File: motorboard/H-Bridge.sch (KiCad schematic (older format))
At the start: 5 parts

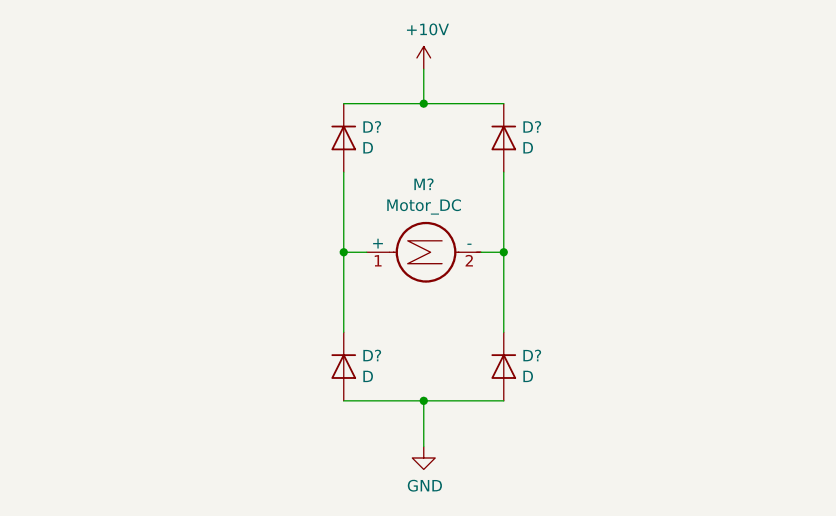
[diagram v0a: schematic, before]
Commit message: basic h bridge complete
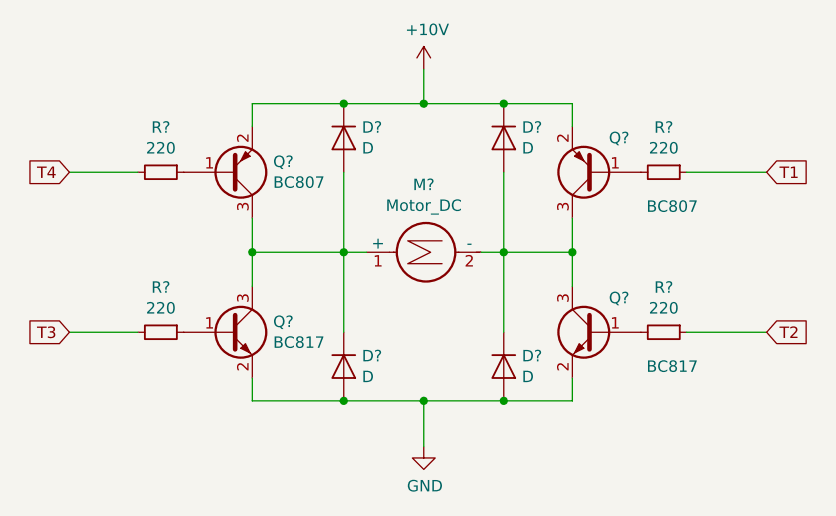
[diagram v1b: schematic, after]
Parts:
- added Q? (x2): BC807, Package_TO_SOT_SMD:SOT-23, symbol Transistor_BJT:BC807
- added Q? (x2): BC817, Package_TO_SOT_SMD:SOT-23, symbol Transistor_BJT:BC817
- added R? (x4): 220, symbol Device:R_Small
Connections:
- net +10V: now also Q?.2 (E), Q?.2 (E)
- net GND: now also Q?.2 (E), Q?.2 (E)
- net at D?.1 (K), D?.2 (A), M?.1 (+): now also Q?.3 (C), Q?.3 (C)
- net at D?.1 (K), D?.2 (A), M?.2 (-): now also Q?.3 (C), Q?.3 (C)
- new net: Q?.1 (B), R?.1 (x2)
- new net: Q?.1 (B), R?.2 (x2)
- new net T1: R?.1
- new net T2: R?.1
- new net T3: R?.2
- new net T4: R?.2
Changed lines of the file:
@@
 U 1 1 5E41C8CC
 P 3800 3350
+AR Path="/5E41C8CC" Ref="M?"  Part="1"
+AR Path="/5E41532A/5E41C8CC" Ref="M?"  Part="1"
 F 0 "M?" V 4095 3300 50  0000 C CNN
 F 1 "Motor_DC" V 4004 3300 50  0000 C CNN
@@
 U 1 1 5E41C8D2
 P 3500 2850
+AR Path="/5E41C8D2" Ref="D?"  Part="1"
+AR Path="/5E41532A/5E41C8D2" Ref="D?"  Part="1"
 F 0 "D?" V 3454 2929 50  0000 L CNN
 F 1 "D" V 3545 2929 50  0000 L CNN
@@
 U 1 1 5E41C8D8
 P 4200 2850
+AR Path="/5E41C8D8" Ref="D?"  Part="1"
+AR Path="/5E41532A/5E41C8D8" Ref="D?"  Part="1"
 F 0 "D?" V 4154 2929 50  0000 L CNN
 F 1 "D" V 4245 2929 50  0000 L CNN
@@
 U 1 1 5E41C8DE
 P 3500 3850
+AR Path="/5E41C8DE" Ref="D?"  Part="1"
+AR Path="/5E41532A/5E41C8DE" Ref="D?"  Part="1"
 F 0 "D?" V 3454 3929 50  0000 L CNN
 F 1 "D" V 3545 3929 50  0000 L CNN
@@
 U 1 1 5E41C8E4
 P 4200 3850
+AR Path="/5E41C8E4" Ref="D?"  Part="1"
+AR Path="/5E41532A/5E41C8E4" Ref="D?"  Part="1"
 F 0 "D?" V 4154 3929 50  0000 L CNN
 F 1 "D" V 4245 3929 50  0000 L CNN
@@
 U 1 1 5E41C8EA
 P 3850 4200
+AR Path="/5E41C8EA" Ref="#PWR?"  Part="1"
+AR Path="/5E41532A/5E41C8EA" Ref="#PWR?"  Part="1"
 F 0 "#PWR?" H 3850 3950 50  0001 C CNN
 F 1 "GND" H 3855 4027 50  0000 C CNN
@@
 AR Path="/5DAD2180/5E41C8F0" Ref="#PWR?"  Part="1"
 AR Path="/5E41C8F0" Ref="#PWR?"  Part="1"
+AR Path="/5E41532A/5E41C8F0" Ref="#PWR?"  Part="1"
 F 0 "#PWR?" H 3850 2400 50  0001 C CNN
 F 1 "+10V" H 3865 2723 50  0000 C CNN
@@
 Wire Wire Line
 	3850 4000 4200 4000
+$Comp
+L Transistor_BJT:BC807 Q?
+U 1 1 5E420AAC
+P 3000 3000
+F 0 "Q?" H 3191 2954 50  0000 L CNN
+F 1 "BC807" H 3191 3045 50  0000 L CNN
+F 2 "Package_TO_SOT_SMD:SOT-23" H 3200 2925 50  0001 L CIN
+F 3 "http://www.fairchildsemi.com/ds/BC/BC807.pdf" H 3000 3000 50  0001 L CNN
+	1    3000 3000
+	1    0    0    1
+$EndComp
+$Comp
+L Transistor_BJT:BC807 Q?
+U 1 1 5E421FC8
+P 4600 3000
+F 0 "Q?" H 4450 2850 50  0000 L CNN
+F 1 "BC807" H 4150 3150 50  0000 L CNN
+F 2 "Package_TO_SOT_SMD:SOT-23" H 4800 2925 50  0001 L CIN
+F 3 "http://www.fairchildsemi.com/ds/BC/BC807.pdf" H 4600 3000 50  0001 L CNN
+	1    4600 3000
+	-1   0    0    1
+$EndComp
+$Comp
+L Transistor_BJT:BC817 Q?
+U 1 1 5E423092
+P 3000 3700
+F 0 "Q?" H 3191 3746 50  0000 L CNN
+F 1 "BC817" H 3191 3655 50  0000 L CNN
+F 2 "Package_TO_SOT_SMD:SOT-23" H 3200 3625 50  0001 L CIN
+F 3 "http://www.fairchildsemi.com/ds/BC/BC817.pdf" H 3000 3700 50  0001 L CNN
+	1    3000 3700
+	1    0    0    -1
+$EndComp
+$Comp
+L Transistor_BJT:BC817 Q?
+U 1 1 5E423BF2
+P 4600 3700
+F 0 "Q?" H 4450 3850 50  0000 L CNN
+F 1 "BC817" H 4150 3550 50  0000 L CNN
+F 2 "Package_TO_SOT_SMD:SOT-23" H 4800 3625 50  0001 L CIN
+F 3 "http://www.fairchildsemi.com/ds/BC/BC817.pdf" H 4600 3700 50  0001 L CNN
+	1    4600 3700
+	-1   0    0    -1
+$EndComp
+Wire Wire Line
+	3100 3500 3100 3350
+Wire Wire Line
+	3500 3350 3100 3350
+Connection ~ 3100 3350
+Wire Wire Line
+	3100 3350 3100 3200
+Wire Wire Line
+	4200 3350 4500 3350
+Wire Wire Line
+	4500 3350 4500 3200
+Wire Wire Line
+	4500 3350 4500 3500
+Connection ~ 4500 3350
+Wire Wire Line
+	4500 3900 4500 4000
+Wire Wire Line
+	4500 4000 4200 4000
+Connection ~ 4200 4000
+Wire Wire Line
+	3500 4000 3100 4000
+Wire Wire Line
+	3100 4000 3100 3900
+Connection ~ 3500 4000
+Wire Wire Line
+	3100 2800 3100 2700
+Wire Wire Line
+	3100 2700 3500 2700
+Connection ~ 3500 2700
+Wire Wire Line
+	4200 2700 4500 2700
+Wire Wire Line
+	4500 2700 4500 2800
+Connection ~ 4200 2700
+$Comp
+L Device:R_Small R?
+U 1 1 5E429C90
+P 2700 3000
+F 0 "R?" V 2504 3000 50  0000 C CNN
+F 1 "220" V 2595 3000 50  0000 C CNN
+F 2 "" H 2700 3000 50  0001 C CNN
+F 3 "~" H 2700 3000 50  0001 C CNN
+	1    2700 3000
+	0    1    1    0
+$EndComp
+$Comp
+L Device:R_Small R?
+U 1 1 5E42A7AD
+P 2700 3700
+F 0 "R?" V 2504 3700 50  0000 C CNN
+F 1 "220" V 2595 3700 50  0000 C CNN
+F 2 "" H 2700 3700 50  0001 C CNN
+F 3 "~" H 2700 3700 50  0001 C CNN
+	1    2700 3700
+	0    1    1    0
+$EndComp
+$Comp
+L Device:R_Small R?
+U 1 1 5E42ACB2
+P 4900 3000
+F 0 "R?" V 4704 3000 50  0000 C CNN
+F 1 "220" V 4795 3000 50  0000 C CNN
+F 2 "" H 4900 3000 50  0001 C CNN
+F 3 "~" H 4900 3000 50  0001 C CNN
+	1    4900 3000
+	0    1    1    0
+$EndComp
+$Comp
+L Device:R_Small R?
+U 1 1 5E42B282
+P 4900 3700
+F 0 "R?" V 4704 3700 50  0000 C CNN
+F 1 "220" V 4795 3700 50  0000 C CNN
+F 2 "" H 4900 3700 50  0001 C CNN
+F 3 "~" H 4900 3700 50  0001 C CNN
+	1    4900 3700
+	0    1    1    0
+$EndComp
+Wire Wire Line
+	2600 3000 2300 3000
+Wire Wire Line
+	2600 3700 2300 3700
+Wire Wire Line
+	5000 3700 5350 3700
+Wire Wire Line
+	5000 3000 5350 3000
+Text GLabel 5350 3000 2    50   Input ~ 0
+T1
+Text GLabel 5350 3700 2    50   Input ~ 0
+T2
+Text GLabel 2300 3700 0    50   Input ~ 0
+T3
+Text GLabel 2300 3000 0    50   Input ~ 0
+T4
 $EndSCHEMATC

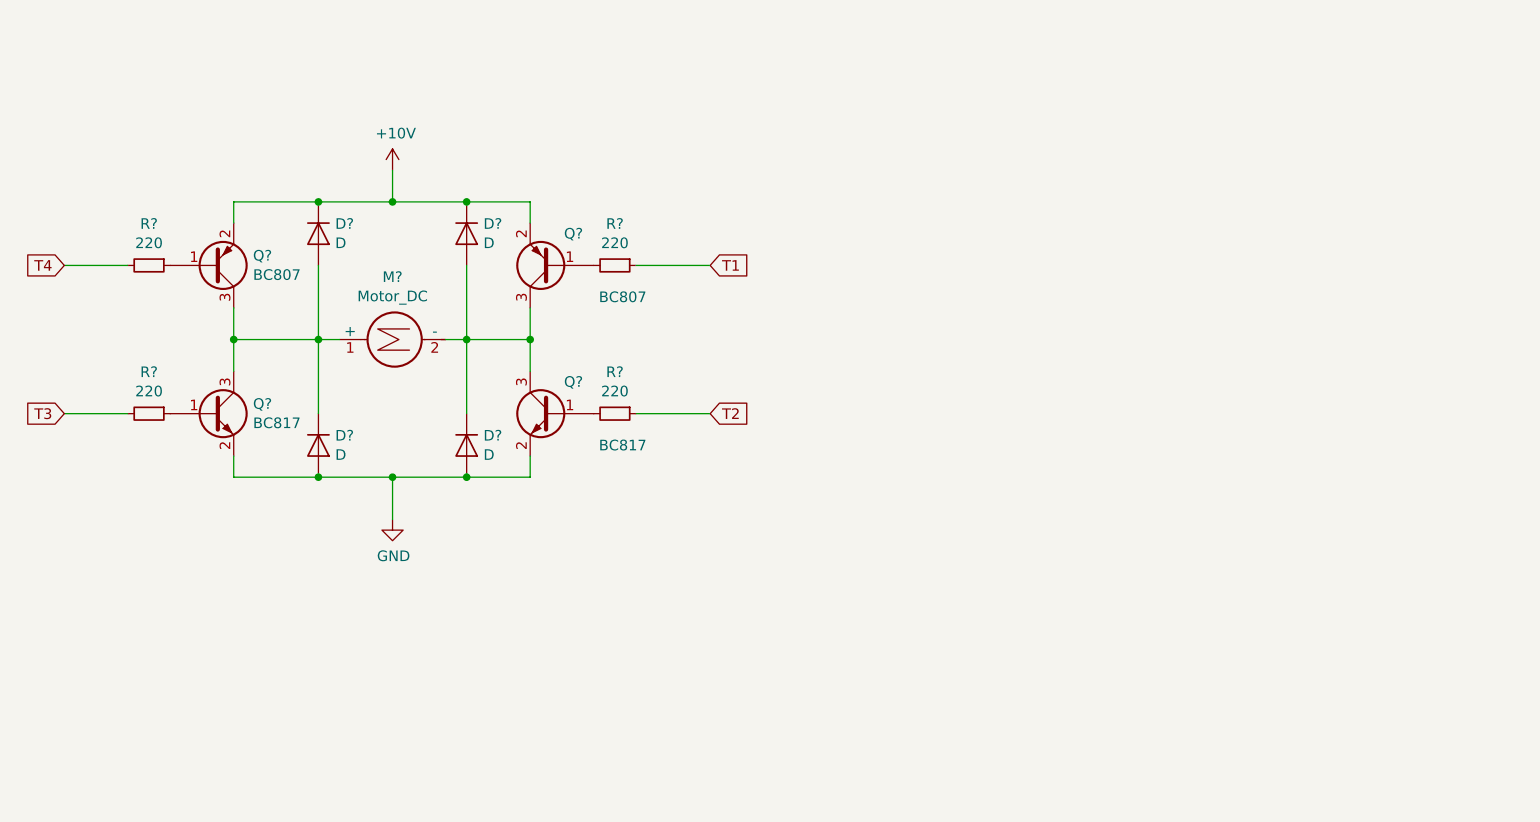
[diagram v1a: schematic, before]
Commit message: Switched to TB6612
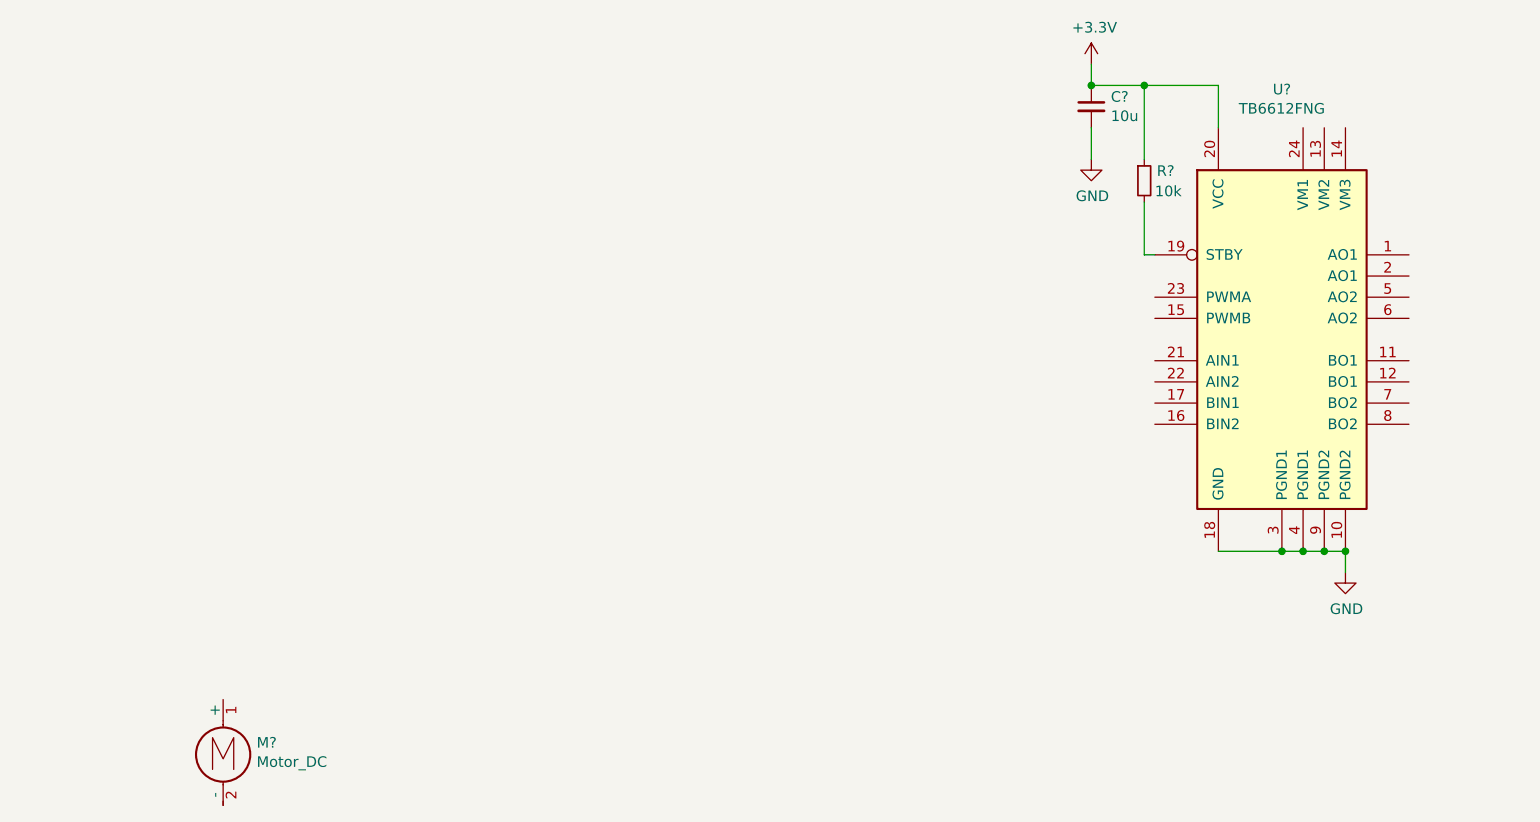
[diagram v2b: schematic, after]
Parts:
- removed D? (x4): D, symbol Device:D
- removed M?: Motor_DC, symbol Motor:Motor_DC
- removed Q? (x2): BC807, Package_TO_SOT_SMD:SOT-23, symbol Transistor_BJT:BC807
- removed Q? (x2): BC817, Package_TO_SOT_SMD:SOT-23, symbol Transistor_BJT:BC817
- removed R? (x4): 220, symbol Device:R_Small
- added C?: 10u, symbol Device:C_Small
- added M?: Motor_DC, Connector_PinSocket_2.00mm:PinSocket_1x01_P2.00mm_Vertical, symbol Motor:Motor_DC
- added R?: 10k, symbol Device:R_Small
- added U?: TB6612FNG, Package_SO:SSOP-24_5.3x8.2mm_P0.65mm, symbol Driver_Motor:TB6612FNG
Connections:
- net GND: now also C?.2, U?.10 (PGND2), U?.18 (GND), U?.3 (PGND1), U?.4 (PGND1), U?.9 (PGND2)
- new net: R?.2, U?.19 (STBY)
- new net +3V3: C?.1, R?.1, U?.20 (VCC)

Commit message: H-bridge setup complete
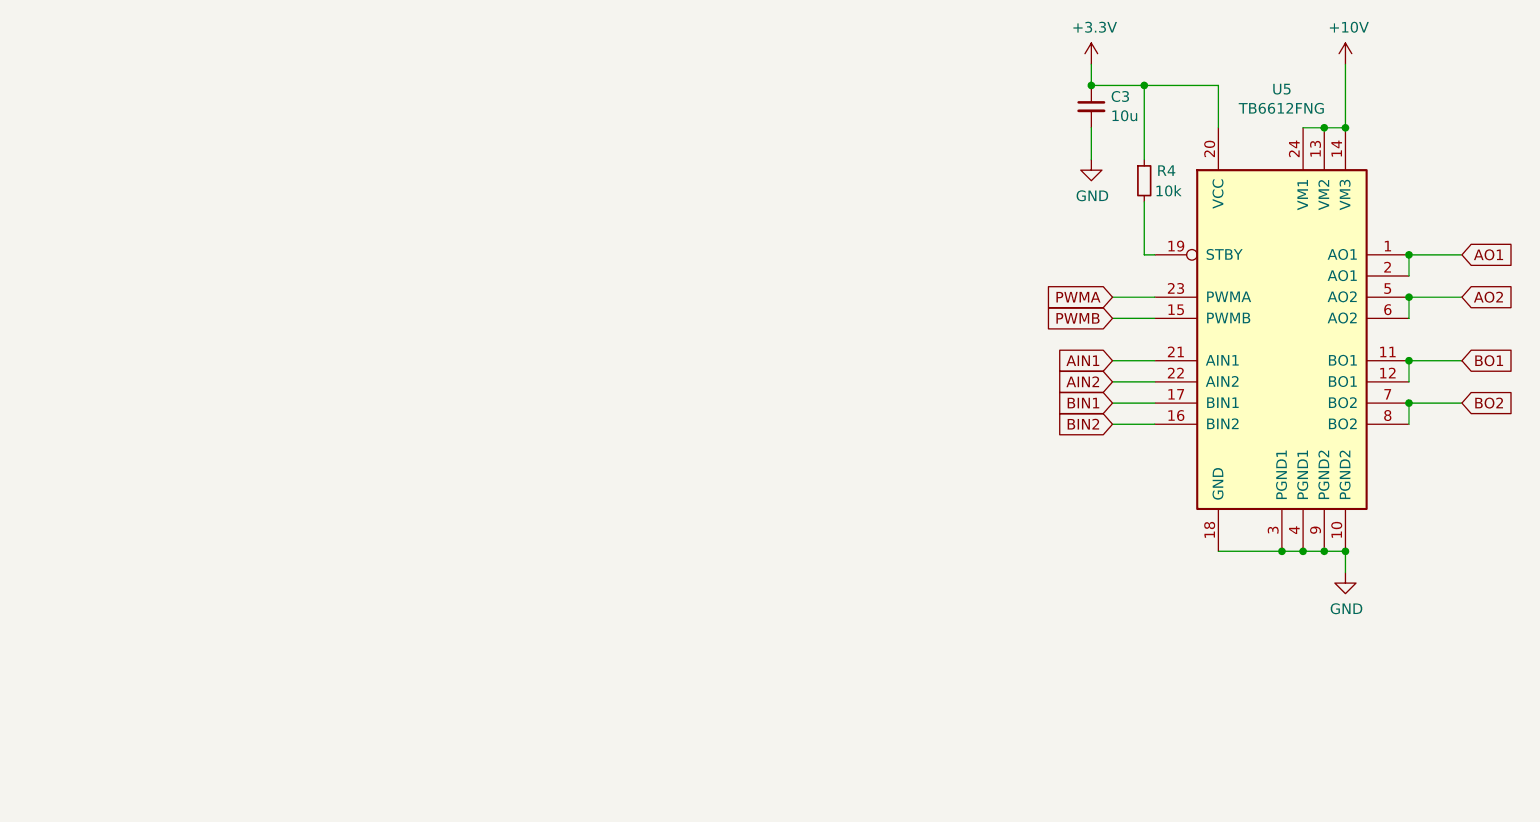
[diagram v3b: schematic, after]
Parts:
- removed M?: Motor_DC, Connector_PinSocket_2.00mm:PinSocket_1x01_P2.00mm_Vertical, symbol Motor:Motor_DC
- gave numbers to parts that had none: 3
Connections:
- net AO1: now reaches U5.1 (AO1)
- net AO1: now also U5.2 (AO1)
- net BO1: now reaches U5.11 (BO1)
- net BO1: now also U5.12 (BO1)
- net +10V: now reaches U5.13 (VM2)
- net +10V: now also U5.14 (VM3), U5.24 (VM1)
- net PWMB: now reaches U5.15 (PWMB)
- net BIN2: now reaches U5.16 (BIN2)
- net BIN1: now reaches U5.17 (BIN1)
- net AIN1: now reaches U5.21 (AIN1)
- net AIN2: now reaches U5.22 (AIN2)
- net PWMA: now reaches U5.23 (PWMA)
- net AO2: now reaches U5.5 (AO2)
- net AO2: now also U5.6 (AO2)
- net BO2: now reaches U5.7 (BO2)
- net BO2: now also U5.8 (BO2)
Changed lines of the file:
@@
 $EndDescr
 $Comp
-L Driver_Motor:TB6612FNG U?
+L Driver_Motor:TB6612FNG U5
 U 1 1 5E36F8D3
 P 8050 3350
-F 0 "U?" H 8050 4531 50  0000 C CNN
+F 0 "U5" H 8050 4531 50  0000 C CNN
 F 1 "TB6612FNG" H 8050 4440 50  0000 C CNN
 F 2 "Package_SO:SSOP-24_5.3x8.2mm_P0.65mm" H 8500 3950 50  0001 C CNN
@@
 	8250 4350 8350 4350
 $Comp
-L power:GND #PWR?
+L power:GND #PWR0117
 U 1 1 5E3711A1
 P 8350 4450
-F 0 "#PWR?" H 8350 4200 50  0001 C CNN
+F 0 "#PWR0117" H 8350 4200 50  0001 C CNN
 F 1 "GND" H 8355 4277 50  0000 C CNN
 F 2 "" H 8350 4450 50  0001 C CNN
@@
 Connection ~ 8050 4350
 $Comp
-L power:+3.3V #PWR?
+L power:+3.3V #PWR0118
 U 1 1 5E3739DF
 P 7150 2050
-F 0 "#PWR?" H 7150 1900 50  0001 C CNN
+F 0 "#PWR0118" H 7150 1900 50  0001 C CNN
 F 1 "+3.3V" H 7165 2223 50  0000 C CNN
 F 2 "" H 7150 2050 50  0001 C CNN
@@
 $EndComp
 $Comp
-L Device:C_Small C?
+L Device:C_Small C3
 U 1 1 5E374198
 P 7150 2250
-F 0 "C?" H 7242 2296 50  0000 L CNN
+F 0 "C3" H 7242 2296 50  0000 L CNN
 F 1 "10u" H 7242 2205 50  0000 L CNN
 F 2 "" H 7150 2250 50  0001 C CNN
@@
 $EndComp
 $Comp
-L power:GND #PWR?
+L power:GND #PWR0119
 U 1 1 5E374E93
 P 7150 2500
-F 0 "#PWR?" H 7150 2250 50  0001 C CNN
+F 0 "#PWR0119" H 7150 2250 50  0001 C CNN
 F 1 "GND" H 7155 2327 50  0000 C CNN
 F 2 "" H 7150 2500 50  0001 C CNN
@@
 	7750 2150 7750 2350
 $Comp
-L Device:R_Small R?
+L Device:R_Small R4
 U 1 1 5E375898
 P 7400 2600
-F 0 "R?" H 7459 2646 50  0000 L CNN
+F 0 "R4" H 7459 2646 50  0000 L CNN
 F 1 "10k" H 7450 2550 50  0000 L CNN
 F 2 "" H 7400 2600 50  0001 C CNN
@@
 Wire Wire Line
 	7400 2950 7450 2950
+Wire Wire Line
+	8150 2350 8250 2350
+Connection ~ 8250 2350
+Wire Wire Line
+	8250 2350 8350 2350
 $Comp
-L Motor:Motor_DC M?
-U 1 1 5E3797EE
-P 3050 5250
-F 0 "M?" H 3208 5246 50  0000 L CNN
-F 1 "Motor_DC" H 3208 5155 50  0000 L CNN
-F 2 "Connector_PinSocket_2.00mm:PinSocket_1x01_P2.00mm_Vertical" H 3050 5160 50  0001 C CNN
-F 3 "~" H 3050 5160 50  0001 C CNN
-	1    3050 5250
+L power:+10V #PWR0120
+U 1 1 5E37F851
+P 8350 2050
+F 0 "#PWR0120" H 8350 1900 50  0001 C CNN
+F 1 "+10V" H 8365 2223 50  0000 C CNN
+F 2 "" H 8350 2050 50  0001 C CNN
+F 3 "" H 8350 2050 50  0001 C CNN
+	1    8350 2050
 	1    0    0    -1
 $EndComp
+Wire Wire Line
+	8350 2350 8350 2050
+Connection ~ 8350 2350
+Wire Wire Line
+	7450 3150 7250 3150
+Wire Wire Line
+	7450 3250 7250 3250
+Wire Wire Line
+	7450 3450 7250 3450
+Wire Wire Line
+	7450 3550 7250 3550
+Wire Wire Line
+	7450 3650 7250 3650
+Wire Wire Line
+	7450 3750 7250 3750
+Wire Wire Line
+	8650 2950 8650 3050
+Wire Wire Line
+	8650 3150 8650 3250
+Wire Wire Line
+	8650 3450 8650 3550
+Wire Wire Line
+	8650 3650 8650 3750
+Wire Wire Line
+	8650 2950 8900 2950
+Connection ~ 8650 2950
+Wire Wire Line
+	8650 3150 8900 3150
+Connection ~ 8650 3150
+Wire Wire Line
+	8650 3450 8900 3450
+Connection ~ 8650 3450
+Wire Wire Line
+	8650 3650 8900 3650
+Connection ~ 8650 3650
+Text GLabel 7250 3150 0    50   Input ~ 0
+PWMA
+Text GLabel 7250 3250 0    50   Input ~ 0
+PWMB
+Text GLabel 7250 3450 0    50   Input ~ 0
+AIN1
+Text GLabel 7250 3550 0    50   Input ~ 0
+AIN2
+Text GLabel 7250 3650 0    50   Input ~ 0
+BIN1
+Text GLabel 7250 3750 0    50   Input ~ 0
+BIN2
+Text GLabel 8900 2950 2    50   Input ~ 0
+AO1
+Text GLabel 8900 3150 2    50   Input ~ 0
+AO2
+Text GLabel 8900 3450 2    50   Input ~ 0
+BO1
+Text GLabel 8900 3650 2    50   Input ~ 0
+BO2
 $EndSCHEMATC
